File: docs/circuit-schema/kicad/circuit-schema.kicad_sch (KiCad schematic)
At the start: 3 parts, among them U1 ESP32-DevKitC, U2 DHT11, U3 MCP3008

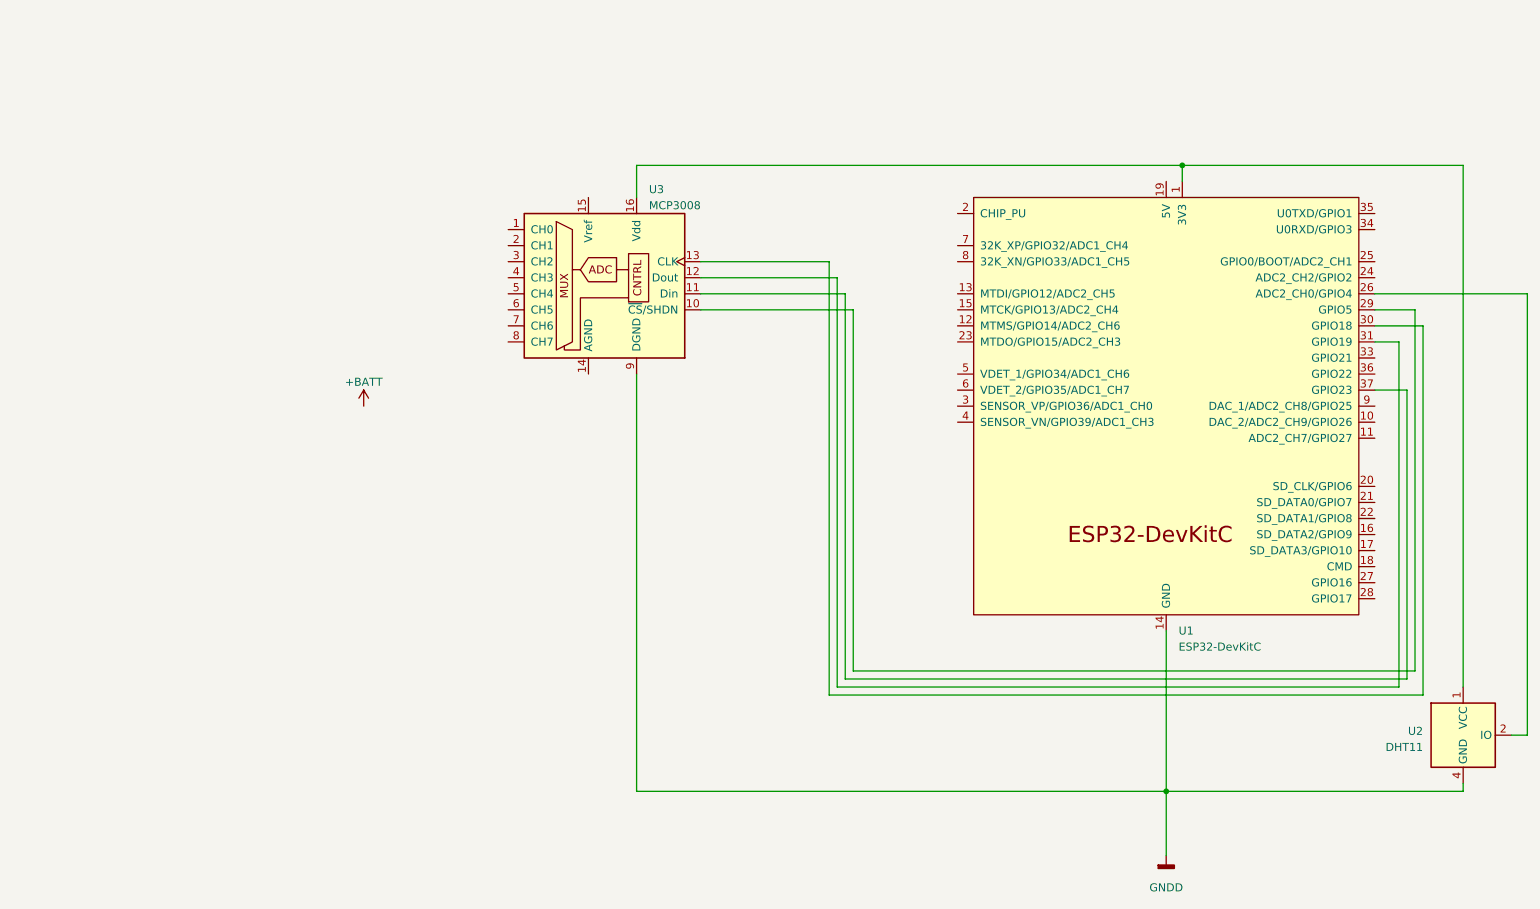
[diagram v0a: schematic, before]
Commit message: Git submodule for CO Sensor KiCad library and further schematic work.
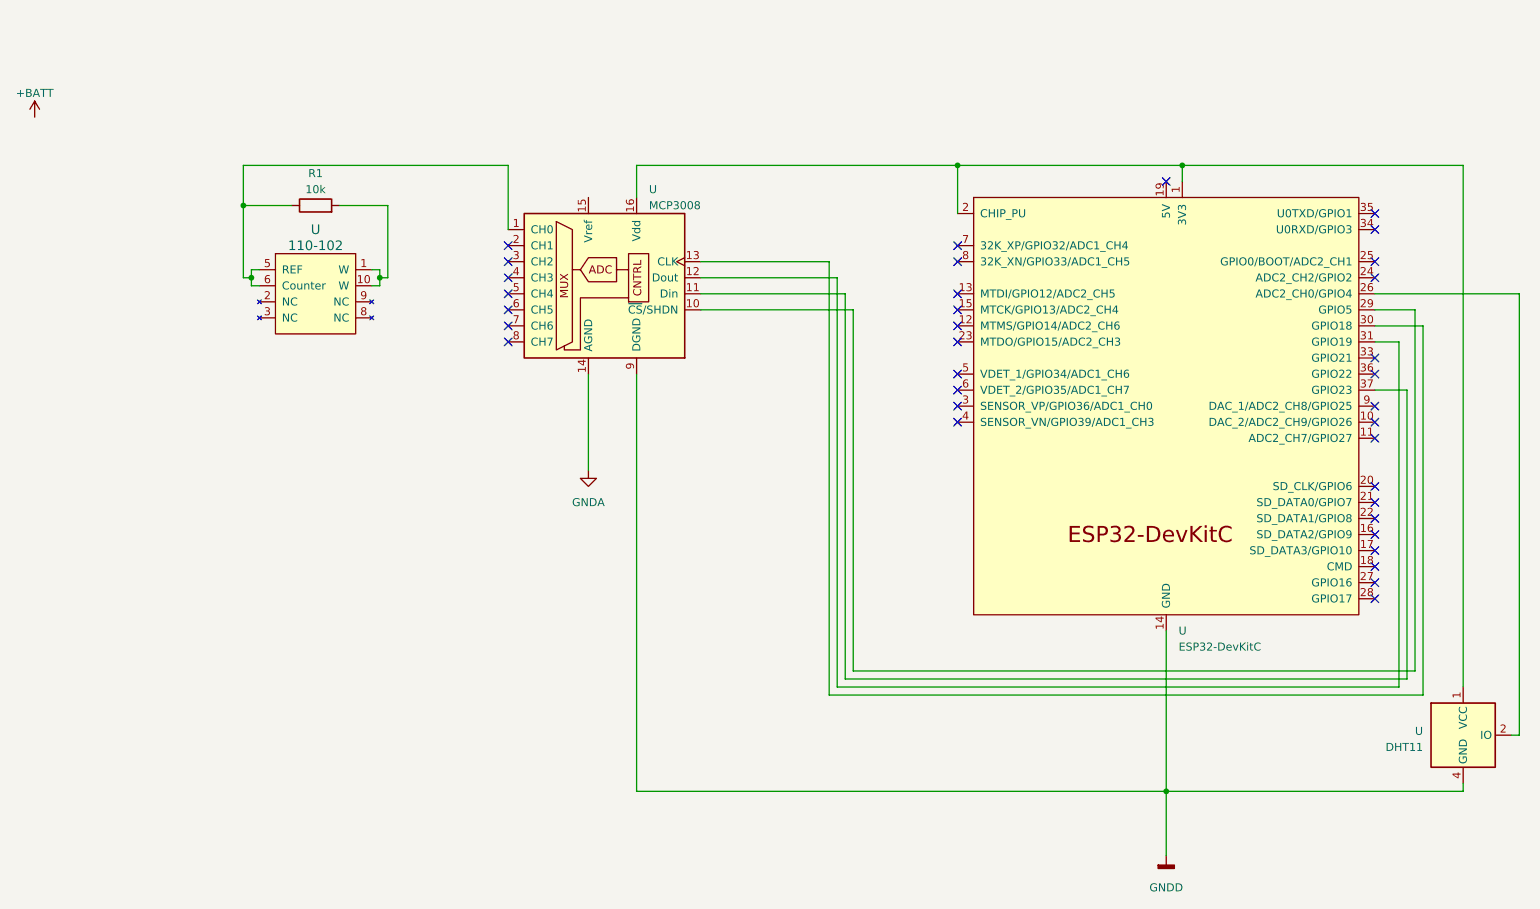
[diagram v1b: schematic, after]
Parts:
- added R1: 10k, symbol Device:R
- added U: 110-102, digikey-footprints:Gas_Sensor_110-109, symbol Digikey gas sensors:110-109
- renumbered U1 to U, U2 to U, U3 to U
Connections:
- net at U.1 (3V3), U.1 (VCC), U.16 (Vdd): now also U.2 (CHIP_PU)
- net at U.1 (CH0): now also R1.1, U.5 (REF), U.6 (Counter)
- net GNDA: now reaches U.14 (AGND)
- new net: R1.2, U.1 (W), U.10 (W)
- no-connect marks 0 -> 35

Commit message: Created custom ISL60002 symbol and MVP for schema.
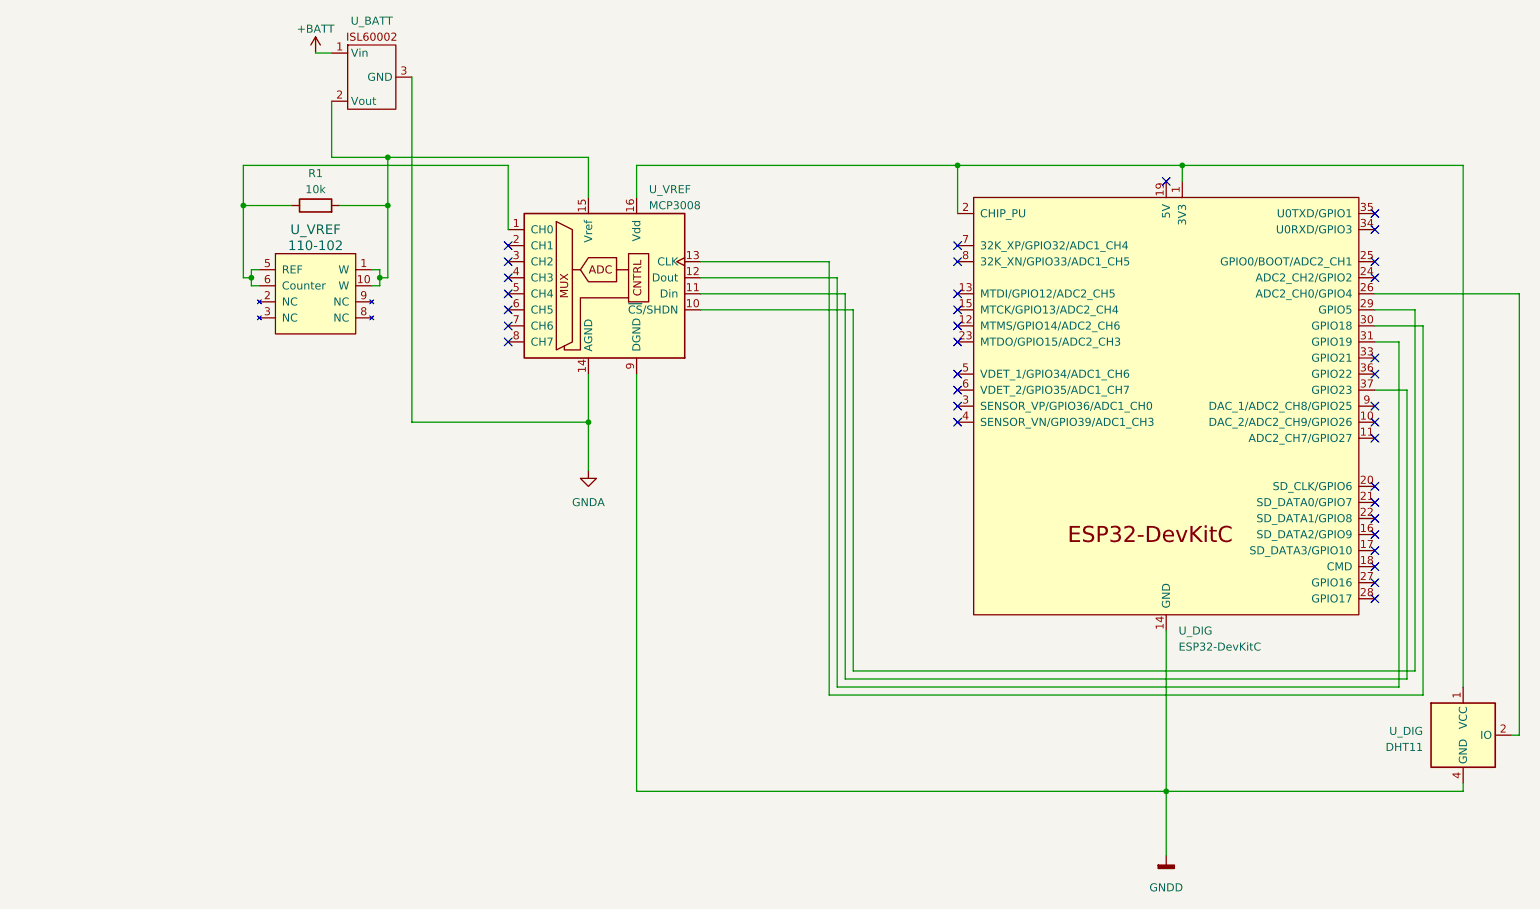
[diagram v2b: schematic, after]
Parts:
- added U_BATT: ~, symbol ISL60002:ISL60002
- renumbered U to U_DIG, U to U_VREF
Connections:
- net +BATT: now also U_BATT.1 (Vin)
- net GNDA: now also U_BATT.3 (GND)
- net at U_VREF.15 (Vref): now also R1.2, U_VREF.1 (W), U_VREF.10 (W), U_BATT.2 (Vout)
